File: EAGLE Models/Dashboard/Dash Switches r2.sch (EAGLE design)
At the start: 26 parts

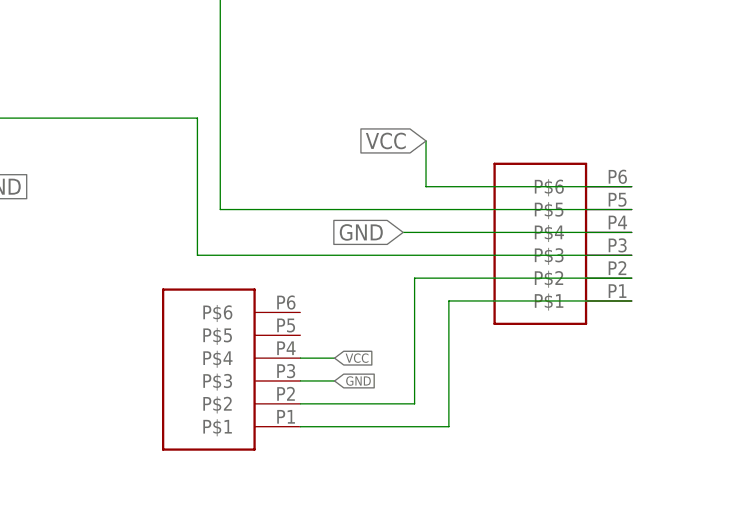
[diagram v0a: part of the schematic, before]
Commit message: Replace connectors with vias for soldering.
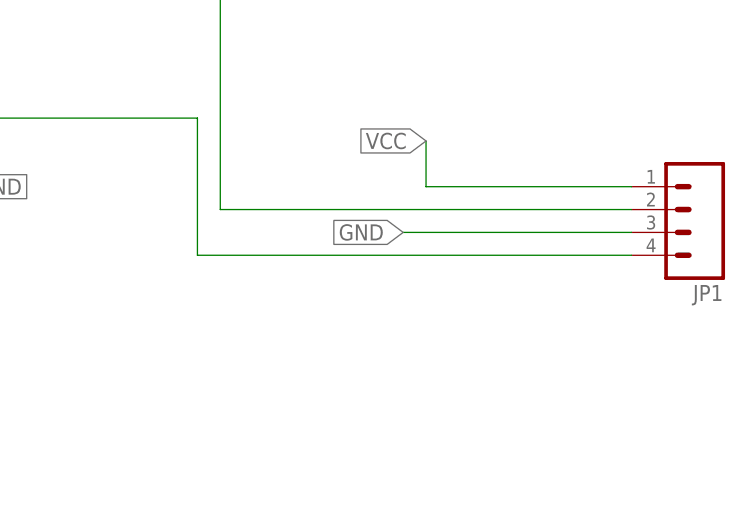
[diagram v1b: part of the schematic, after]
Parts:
- removed U$3, U$6: MICRO6LOCK, DashAndCAN library:MICRO6LOCK
- added JP1: (no value), SparkFun-Connectors:M04LOCK
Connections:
- removed net N$30: U$3.P$2, U$6.P$2
- removed net N$40: U$3.P$1, U$6.P$1
- net GND: now also JP1.3; no longer U$3.P$3, U$6.P$4
- net N$19: now also JP1.4; no longer U$6.P$3
- net N$37: now also JP1.2; no longer U$6.P$5
- net VCC: now also JP1.1; no longer U$3.P$4, U$6.P$6
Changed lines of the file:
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@@
 <setting verticaltext="up"/>
 </settings>
-<grid distance="0.05" unitdist="inch" unit="inch" style="lines" multiple="1" display="no" altdistance="0.01" altunitdist="inch" altunit="inch"/>
+<grid distance="0.1" unitdist="inch" unit="inch" style="lines" multiple="1" display="no" altdistance="0.01" altunitdist="inch" altunit="inch"/>
 <layers>
 <layer number="1" name="Top" color="4" fill="1" visible="no" active="no"/>
@@
 <part name="R20" library="rcl" deviceset="R-US_" device="R0603" value="1k"/>
 <part name="R21" library="rcl" deviceset="R-US_" device="R0603" value="1k"/>
-<part name="U$6" library="DashAndCAN library" deviceset="MICRO6LOCK" device=""/>
-<part name="U$3" library="DashAndCAN library" deviceset="MICRO6LOCK" device=""/>
+<part name="JP1" library="SparkFun-Connectors" deviceset="M04" device="LOCK"/>
 </parts>
 <sheets>
@@
 <instance part="R20" gate="G$1" x="-5.08" y="-64.77"/>
 <instance part="R21" gate="G$1" x="3.81" y="-72.39"/>
-<instance part="U$6" gate="G$1" x="78.74" y="-50.8" rot="R180"/>
-<instance part="U$3" gate="G$1" x="41.91" y="-64.77" rot="R180"/>
+<instance part="JP1" gate="G$1" x="93.98" y="-45.72" rot="R180"/>
 </instances>
 <busses>
@@
 <wire x1="66.04" y1="-43.18" x2="66.04" y2="-38.1" width="0.1524" layer="91"/>
 <label x="66.04" y="-38.1" size="1.778" layer="95" rot="R180" xref="yes"/>
-<pinref part="U$6" gate="G$1" pin="P$6"/>
 <wire x1="66.04" y1="-43.18" x2="88.9" y2="-43.18" width="0.1524" layer="91"/>
+<pinref part="JP1" gate="G$1" pin="1"/>
 </segment>
 <segment>
@@
 <wire x1="-52.07" y1="-45.72" x2="-77.47" y2="-45.72" width="0.1524" layer="91"/>
 <junction x="-77.47" y="-45.72"/>
-</segment>
-<segment>
-<pinref part="U$3" gate="G$1" pin="P$4"/>
-<wire x1="52.07" y1="-62.23" x2="55.88" y2="-62.23" width="0.1524" layer="91"/>
-<label x="55.88" y="-62.23" size="1.016" layer="95" xref="yes"/>
 </segment>
 </net>
@@
 <segment>
 <label x="63.5" y="-48.26" size="1.778" layer="95" rot="R180" xref="yes"/>
-<pinref part="U$6" gate="G$1" pin="P$4"/>
 <wire x1="63.5" y1="-48.26" x2="88.9" y2="-48.26" width="0.1524" layer="91"/>
+<pinref part="JP1" gate="G$1" pin="3"/>
 </segment>
 <segment>
@@
 <wire x1="8.89" y1="-72.39" x2="11.43" y2="-72.39" width="0.1524" layer="91"/>
 </segment>
-<segment>
-<pinref part="U$3" gate="G$1" pin="P$3"/>
-<wire x1="52.07" y1="-64.77" x2="55.88" y2="-64.77" width="0.1524" layer="91"/>
-<label x="55.88" y="-64.77" size="1.016" layer="95" xref="yes"/>
-</segment>
 </net>
 <net name="N$37" class="0">
@@
 <wire x1="43.18" y1="17.78" x2="43.18" y2="-45.72" width="0.1524" layer="91"/>
 <wire x1="43.18" y1="-45.72" x2="88.9" y2="-45.72" width="0.1524" layer="91"/>
-<pinref part="U$6" gate="G$1" pin="P$5"/>
-</segment>
-</net>
-<net name="N$40" class="0">
-<segment>
-<wire x1="68.58" y1="-55.88" x2="68.58" y2="-69.85" width="0.1524" layer="91"/>
-<pinref part="U$6" gate="G$1" pin="P$1"/>
-<wire x1="68.58" y1="-55.88" x2="88.9" y2="-55.88" width="0.1524" layer="91"/>
-<pinref part="U$3" gate="G$1" pin="P$1"/>
-<wire x1="68.58" y1="-69.85" x2="52.07" y2="-69.85" width="0.1524" layer="91"/>
+<pinref part="JP1" gate="G$1" pin="2"/>
 </segment>
 </net>
@@
 <wire x1="88.9" y1="-50.8" x2="40.64" y2="-50.8" width="0.1524" layer="91"/>
 <wire x1="40.64" y1="-50.8" x2="40.64" y2="-35.56" width="0.1524" layer="91"/>
-<pinref part="U$6" gate="G$1" pin="P$3"/>
+<pinref part="JP1" gate="G$1" pin="4"/>
 </segment>
 </net>
@@
 </segment>
 </net>
-<net name="N$30" class="0">
-<segment>
-<pinref part="U$6" gate="G$1" pin="P$2"/>
-<wire x1="64.77" y1="-53.34" x2="88.9" y2="-53.34" width="0.1524" layer="91"/>
-<wire x1="64.77" y1="-67.31" x2="64.77" y2="-53.34" width="0.1524" layer="91"/>
-<pinref part="U$3" gate="G$1" pin="P$2"/>
-<wire x1="64.77" y1="-67.31" x2="52.07" y2="-67.31" width="0.1524" layer="91"/>
-</segment>
-</net>
